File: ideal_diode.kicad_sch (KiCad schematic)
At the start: 15 parts, among them Q1 NVMFS5C404NL, U1 SN74LVC2G08, U2 LM74700

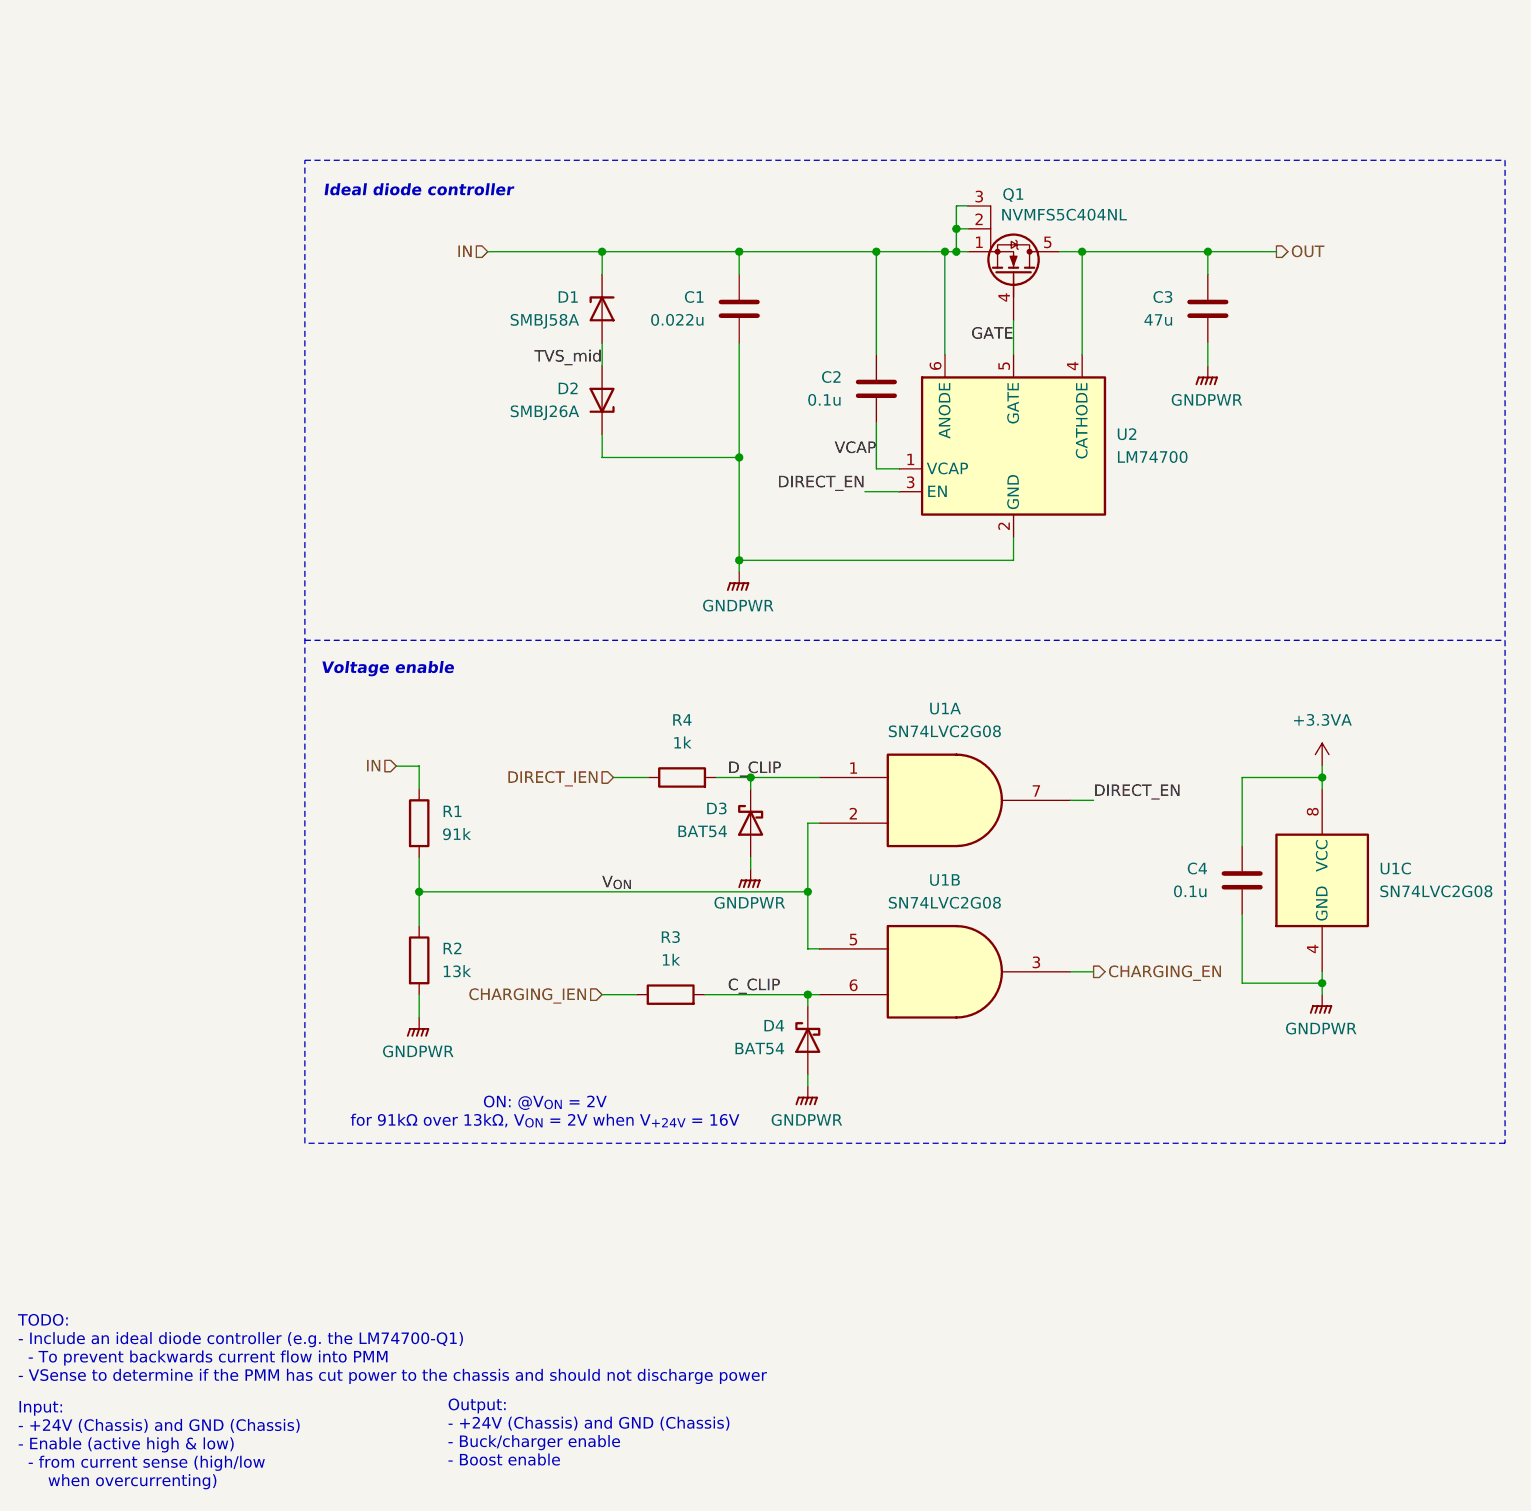
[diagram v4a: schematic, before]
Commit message: Completed stage 2 schematic
+ added SPICE models for all the custom components
+ renumbered components
+ updated library with stage 2 symbols
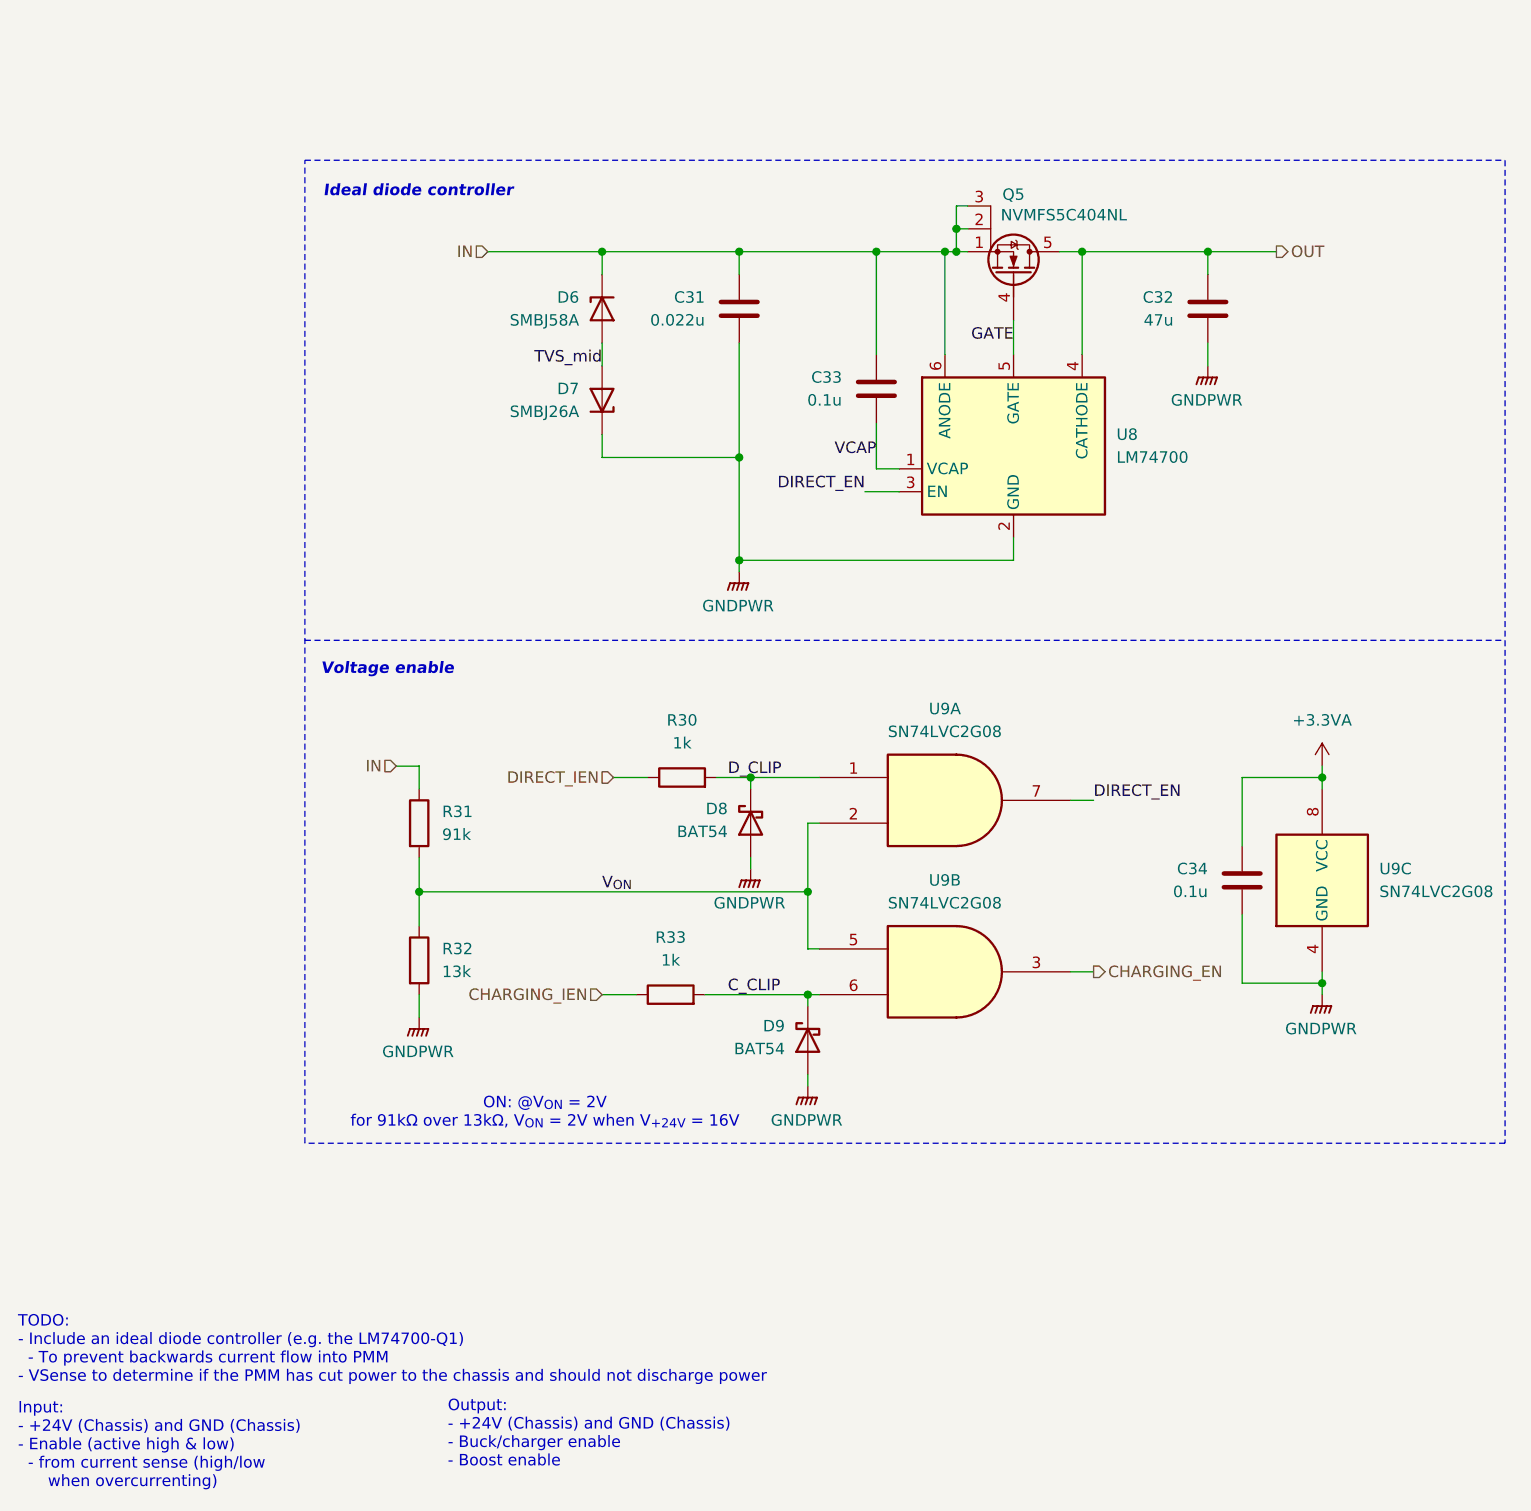
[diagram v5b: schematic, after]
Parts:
- renumbered C1 to C31, C3 to C32, C2 to C33, C4 to C34, D1 to D6, D2 to D7, D3 to D8, D4 to D9, Q1 to Q5, R4 to R30, R1 to R31, R2 to R32, R3 to R33, U2 to U8, U1 to U9
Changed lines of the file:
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@@
 		(dnp no)
 		(fields_autoplaced yes)
-		(property "Reference" "R1"
+		(property "Reference" "R31"
 			(at 91.44 110.4899 0)
 			(effects
@@
 		(dnp no)
 		(fields_autoplaced yes)
-		(property "Reference" "R4"
+		(property "Reference" "R30"
 			(at 118.11 100.33 90)
 			(effects
@@
 		(on_board yes)
 		(dnp no)
-		(property "Reference" "C3"
+		(property "Reference" "C32"
 			(at 172.72 53.3399 0)
 			(effects
@@
 		(on_board yes)
 		(dnp no)
-		(property "Reference" "D3"
+		(property "Reference" "D8"
 			(at 123.19 110.1724 90)
 			(effects
@@
 		(on_board yes)
 		(dnp no)
-		(property "Reference" "C1"
+		(property "Reference" "C31"
 			(at 120.65 53.3399 0)
 			(effects
@@
 		(on_board yes)
 		(dnp no)
-		(property "Reference" "D4"
+		(property "Reference" "D9"
 			(at 129.54 134.3024 90)
 			(effects
@@
 		(dnp no)
 		(fields_autoplaced yes)
-		(property "Reference" "#PWR0102"
+		(property "Reference" "#PWR056"
 			(at 125.73 121.92 0)
 			(effects
@@
 		(dnp no)
 		(fields_autoplaced yes)
-		(property "Reference" "R3"
+		(property "Reference" "R33"
 			(at 116.84 124.46 90)
 			(effects
@@
 		(dnp no)
 		(fields_autoplaced yes)
-		(property "Reference" "U1"
+		(property "Reference" "U9"
 			(at 147.3089 118.11 0)
 			(effects
@@
 		(dnp no)
 		(fields_autoplaced yes)
-		(property "Reference" "#PWR0106"
+		(property "Reference" "#PWR057"
 			(at 189.23 135.89 0)
 			(effects
@@
 		(dnp no)
 		(fields_autoplaced yes)
-		(property "Reference" "#PWR0105"
+		(property "Reference" "#PWR055"
 			(at 189.23 109.22 0)
 			(effects
@@
 		(dnp no)
 		(fields_autoplaced yes)
-		(property "Reference" "#PWR0107"
+		(property "Reference" "#PWR054"
 			(at 124.46 88.9 0)
 			(effects
@@
 		(on_board yes)
 		(dnp no)
-		(property "Reference" "C2"
+		(property "Reference" "C33"
 			(at 135.89 62.2299 0)
 			(effects
@@
 		(on_board yes)
 		(dnp no)
-		(property "Reference" "Q1"
+		(property "Reference" "Q5"
 			(at 154.94 41.91 90)
 			(effects
@@
 		(dnp no)
 		(fields_autoplaced yes)
-		(property "Reference" "U2"
+		(property "Reference" "U8"
 			(at 166.37 68.5799 0)
 			(effects
@@
 		(dnp no)
 		(fields_autoplaced yes)
-		(property "Reference" "U1"
+		(property "Reference" "U9"
 			(at 195.58 116.8399 0)
 			(effects
@@
 		(dnp no)
 		(fields_autoplaced yes)
-		(property "Reference" "R2"
+		(property "Reference" "R32"
 			(at 91.44 125.7299 0)
 			(effects
@@
 		(on_board yes)
 		(dnp no)
-		(property "Reference" "D1"
+		(property "Reference" "D6"
 			(at 106.68 53.3399 90)
 			(effects
@@
 		(dnp no)
 		(fields_autoplaced yes)
-		(property "Reference" "#PWR0104"
+		(property "Reference" "#PWR053"
 			(at 176.53 66.04 0)
 			(effects
@@
 		(on_board yes)
 		(dnp no)
-		(property "Reference" "C4"
+		(property "Reference" "C34"
 			(at 176.53 116.8399 0)
 			(effects
@@
 		(dnp no)
 		(fields_autoplaced yes)
-		(property "Reference" "U1"
+		(property "Reference" "U9"
 			(at 147.3089 99.06 0)
 			(effects
@@
 		(dnp no)
 		(fields_autoplaced yes)
-		(property "Reference" "#PWR0103"
+		(property "Reference" "#PWR058"
 			(at 88.9 138.43 0)
 			(effects
@@
 		(on_board yes)
 		(dnp no)
-		(property "Reference" "D2"
+		(property "Reference" "D7"
 			(at 106.68 63.4999 90)
 			(effects
@@
 		(dnp no)
 		(fields_autoplaced yes)
-		(property "Reference" "#PWR0101"
+		(property "Reference" "#PWR059"
 			(at 132.08 146.05 0)
 			(effects

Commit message: Adding simulation for charging & balancing
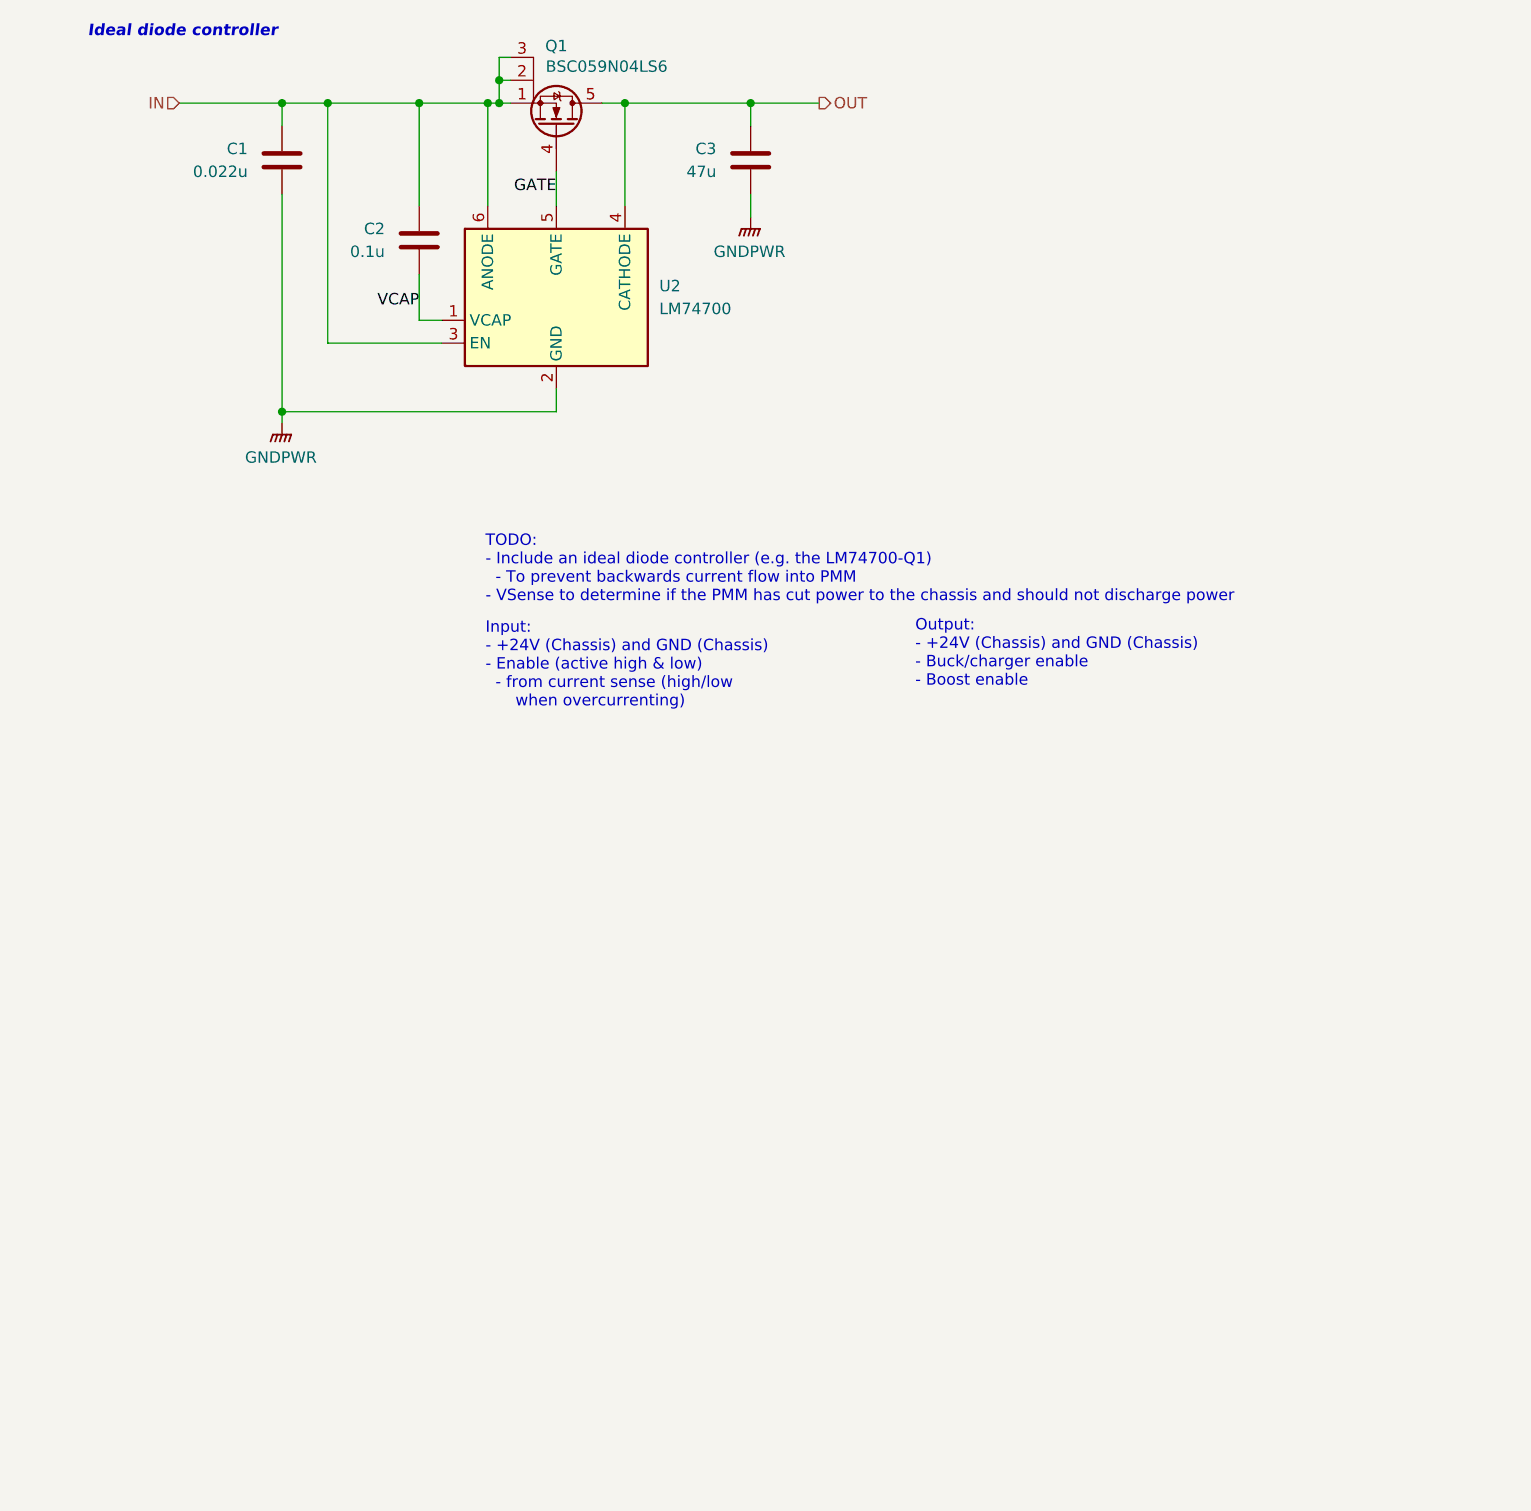
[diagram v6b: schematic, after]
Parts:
- removed C34: 0.1u, Capacitor_SMD:C_0603_1608Metric_Pad1.08x0.95mm_HandSolder, symbol Device:C
- removed D6: SMBJ58A, Diode_SMD:D_SMB_Handsoldering, symbol Device:D_Zener
- removed D7: SMBJ26A, Diode_SMD:D_SMB_Handsoldering, symbol Device:D_Zener
- removed D8, D9: BAT54, Package_TO_SOT_SMD:SOT-23_Handsoldering, symbol Device:D_Schottky
- removed R30, R33: 1k, Resistor_SMD:R_0603_1608Metric_Pad0.98x0.95mm_HandSolder, symbol Device:R
- removed R31: 91k, Resistor_SMD:R_0603_1608Metric_Pad0.98x0.95mm_HandSolder, symbol Device:R
- removed R32: 13k, Resistor_SMD:R_0603_1608Metric_Pad0.98x0.95mm_HandSolder, symbol Device:R
- removed U9: SN74LVC2G08, Package_SO:VSSOP-8_2.3x2mm_P0.5mm, symbol ! Robomaster ICs:SN74LVC2G08
- Q1: renamed from Q5; value NVMFS5C404NL -> BSC059N04LS6; footprint Package_SO:ONSemi_SO-8FL_488AA -> Package_SON:Infineon_PG-TDSON-8_6.15x5.15mm; Mouser Part Number (none) -> 726-BSC059N04LS6ATMA
- renumbered C31 to C1, C33 to C2, C32 to C3, U8 to U2
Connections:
- net DIRECT_EN is gone; now on net IN: U2.3 (EN)
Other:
- note removed: "ON: @V_{ON} = 2V for 91kΩ over 13kΩ, V_{ON} = 2V when V_{+24V} = 16V"
- note removed: "Voltage enable"
- moved on the sheet: C1, C2, C3, Q1, U2
